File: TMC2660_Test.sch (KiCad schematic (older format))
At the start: 50 parts, among them P101 CONN_4, P102 CONN_4, P103 CONN_2, P104 CONN_13X2, P105 CONN_4, P106 CONN_4, U101 TMC2660, U102 TMC2660, U103 TMC2660, U104 TMC2660

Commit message: Halfway done with layout.
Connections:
- net Y-DIR: now also P104.23 (P23); no longer P104.19 (P19)
- net Y-SEL: now also P104.19 (P19); no longer P104.23 (P23)
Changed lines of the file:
@@
 Text GLabel 5500 6950 0    30   Input ~ 0
 Y-EN
-Text GLabel 5500 7050 0    30   Input ~ 0
+Text GLabel 5500 7250 0    30   Input ~ 0
 Y-DIR
 Text GLabel 5500 7150 0    30   Input ~ 0
 Y-STEP
-Text GLabel 5500 7250 0    30   Input ~ 0
+Text GLabel 5500 7050 0    30   Input ~ 0
 Y-SEL
 Text GLabel 6400 6650 2    30   Input ~ 0

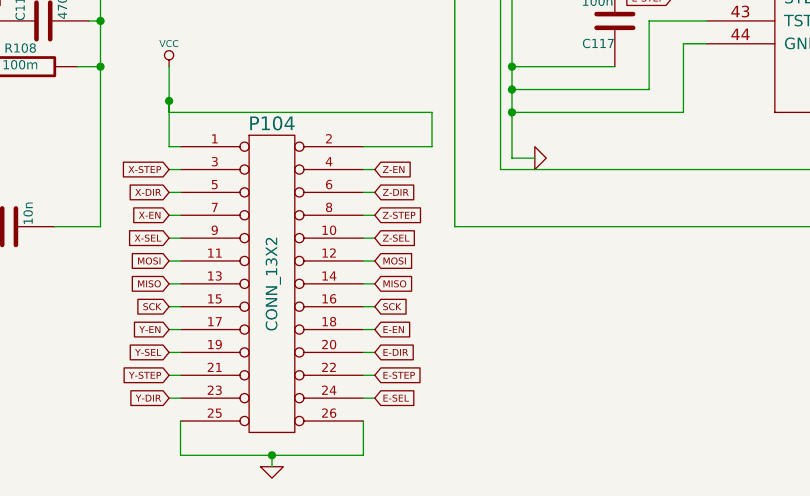
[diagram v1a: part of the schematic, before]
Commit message: Adjust connector to match other side.
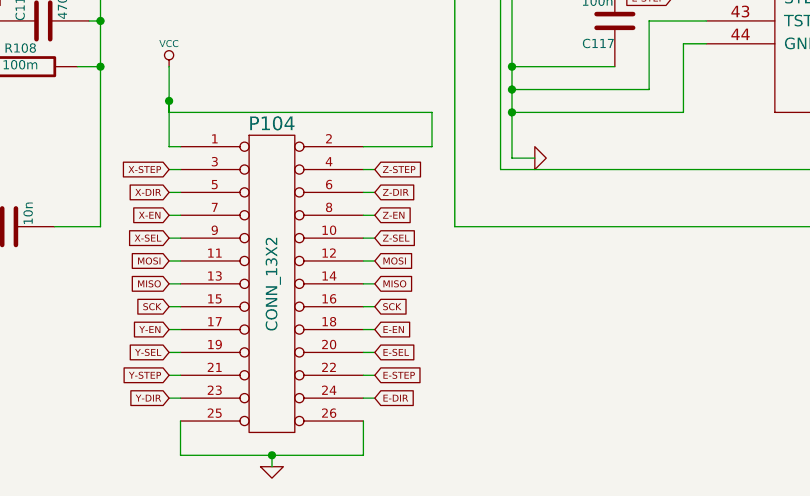
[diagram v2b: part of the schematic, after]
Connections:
- net E-DIR: now also P104.24 (P20); no longer P104.20 (P20)
- net E-SEL: now also P104.20 (P20); no longer P104.24 (P20)
- net Z-EN: now also P104.8 (P8); no longer P104.4 (P4)
- net Z-STEP: now also P104.4 (P4); no longer P104.8 (P8)
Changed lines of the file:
@@
 Text GLabel 6400 6850 2    30   Input ~ 0
 SCK
-Text GLabel 6400 6250 2    30   Input ~ 0
+Text GLabel 6400 6450 2    30   Input ~ 0
 Z-EN
 Text GLabel 6400 6350 2    30   Input ~ 0
 Z-DIR
-Text GLabel 6400 6450 2    30   Input ~ 0
+Text GLabel 6400 6250 2    30   Input ~ 0
 Z-STEP
 Text GLabel 6400 6550 2    30   Input ~ 0
@@
 Text GLabel 6400 6950 2    30   Input ~ 0
 E-EN
-Text GLabel 6400 7050 2    30   Input ~ 0
+Text GLabel 6400 7250 2    30   Input ~ 0
 E-DIR
 Text GLabel 6400 7150 2    30   Input ~ 0
 E-STEP
-Text GLabel 6400 7250 2    30   Input ~ 0
+Text GLabel 6400 7050 2    30   Input ~ 0
 E-SEL
 Wire Wire Line
